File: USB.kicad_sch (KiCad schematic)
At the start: 8 parts

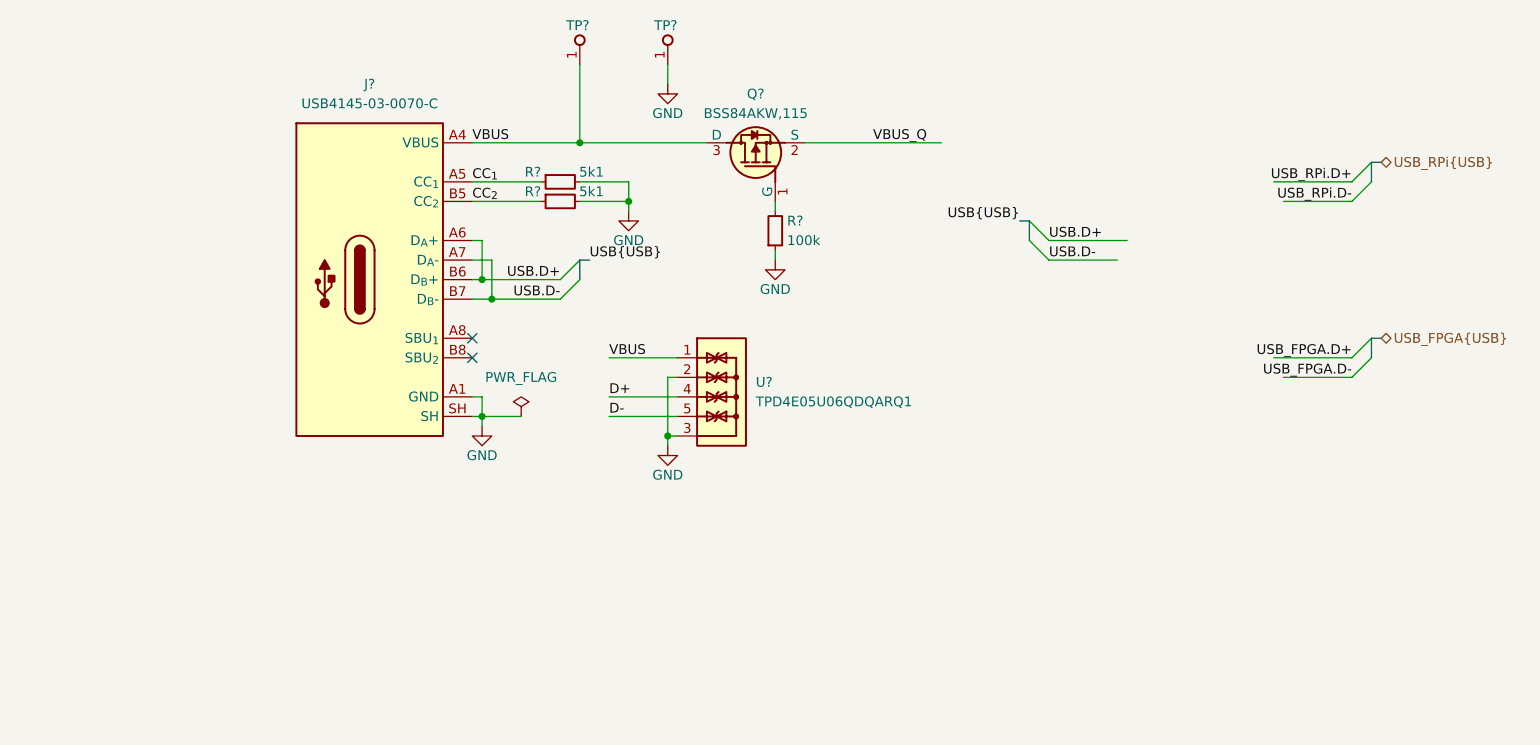
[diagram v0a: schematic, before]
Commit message: [#72133] Add USB mux
Signed-off-by: Dawid Lentka <dlentka@antmicro.com>
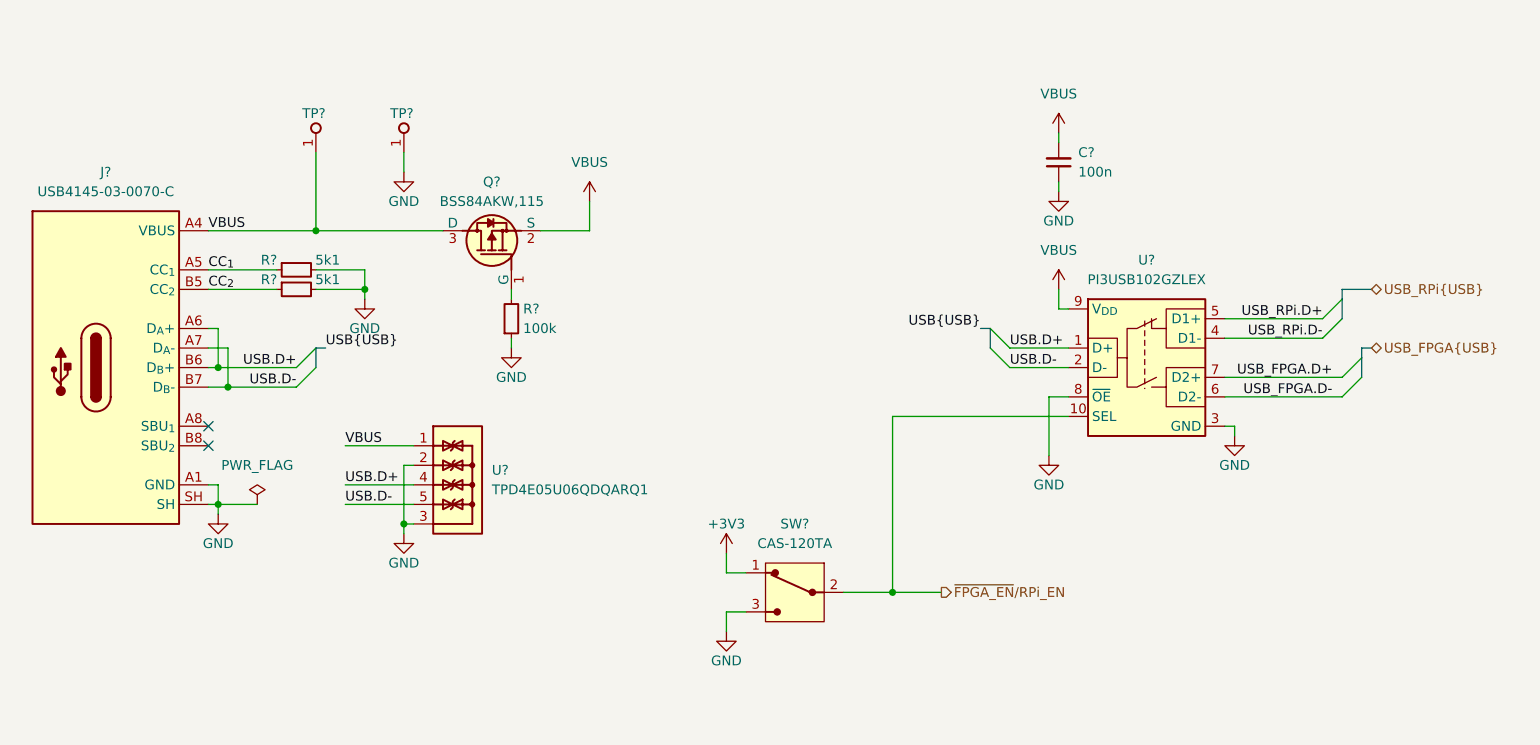
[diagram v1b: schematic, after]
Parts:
- added C?: C_100n_0402, antmicro-footprints:C_0402_1005Metric, symbol antmicroCapacitors0402:C_100n_0402
- added SW?: CAS-120TA, antmicro-footprints:Switch_Slide_CAS-120TA, symbol antmicroSlideSwitches:CAS-120TA
- added U?: PI3USB102GZLEX, antmicro-footprints:UQFN-10_1.4x1.8x0.5mm_P0.4mm, symbol antmicroInterfaceAnalogSwitchesSpecialPurpose:PI3USB102GZLEX
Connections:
- net D+ is gone; now on net USB.D+: U?.4, U?.7
- net D- is gone; now on net USB.D-: U?.5, U?.6
- net VBUS_Q is gone; now on net VBUS: Q?.2 (S)
- net GND: now also C?.1, SW?.3, U?.3 (GND), U?.8 (~{OE})
- net USB.D+: now also U?.1 (D+)
- net USB.D-: now also U?.2 (D-)
- net USB_FPGA.D+: now also U?.7 (D2+)
- net USB_FPGA.D-: now also U?.6 (D2-)
- net USB_RPi.D+: now also U?.5 (D1+)
- net USB_RPi.D-: now also U?.4 (D1-)
- net VBUS: now also C?.2, U?.9 (V_{DD})
- new net +3V3: SW?.1
- new net ~{FPGA_EN}/RPi_EN: SW?.2, U?.10 (SEL)
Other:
- moved on the sheet: J?, Q?, R?, TP?, U?

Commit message: [#72133] Move executor switching to new scheet; Add FPGA flash programmer
Signed-off-by: Dawid Lentka <dlentka@antmicro.com>
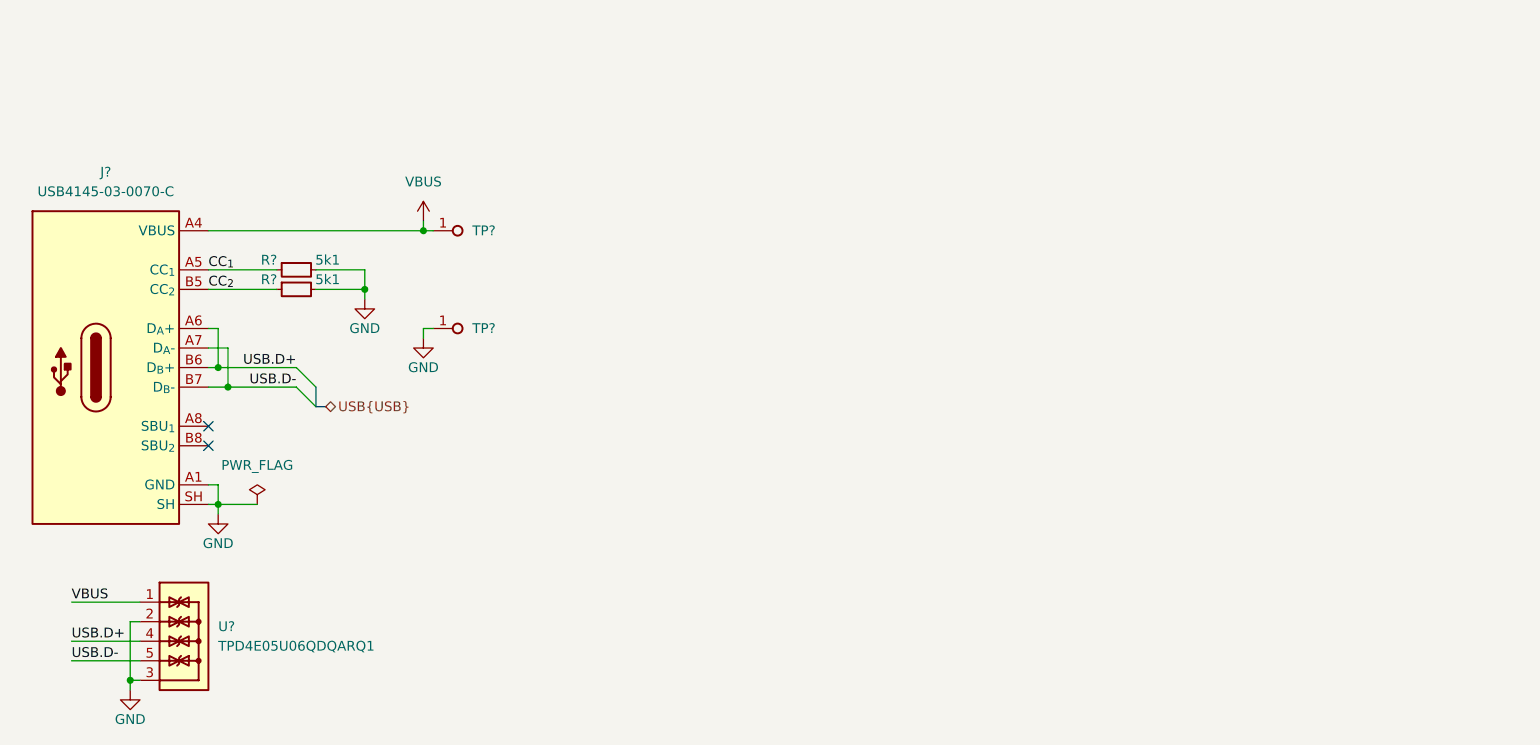
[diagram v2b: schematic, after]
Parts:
- removed C?: C_100n_0402, antmicro-footprints:C_0402_1005Metric, symbol antmicroCapacitors0402:C_100n_0402
- removed Q?: BSS84AKW, antmicro-footprints:SOT-323, symbol antmicroTransistorsFETsMOSFETsSingle:BSS84AKW
- removed R?: R_100k_0402, antmicro-footprints:R_0402_1005Metric, symbol antmicroResistors0402:R_100k_0402
- removed SW?: CAS-120TA, antmicro-footprints:Switch_Slide_CAS-120TA, symbol antmicroSlideSwitches:CAS-120TA
- removed U?: PI3USB102GZLEX, antmicro-footprints:UQFN-10_1.4x1.8x0.5mm_P0.4mm, symbol antmicroInterfaceAnalogSwitchesSpecialPurpose:PI3USB102GZLEX
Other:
- moved on the sheet: TP?, U?

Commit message: [#72133] Unify sheet size
Signed-off-by: Dawid Lentka <dlentka@antmicro.com>
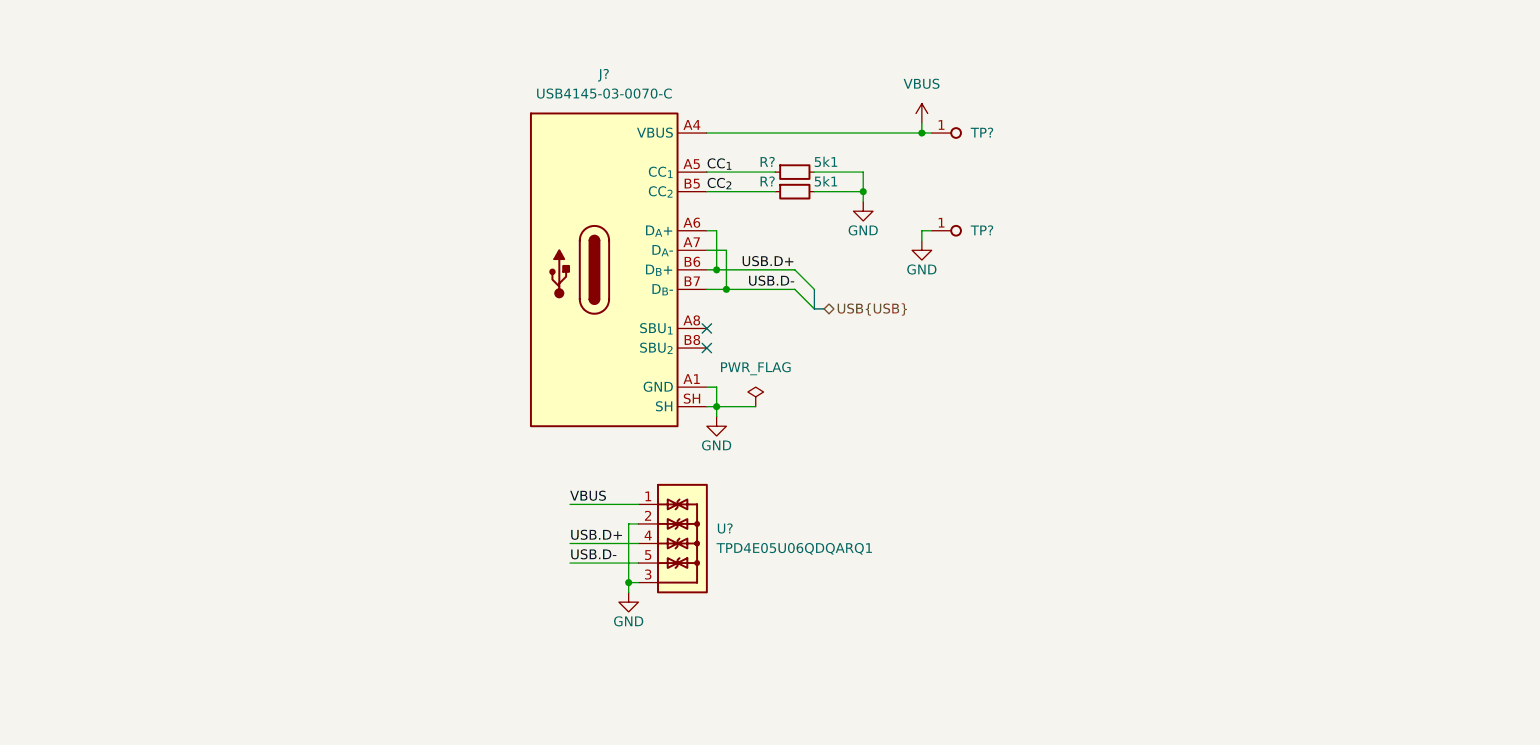
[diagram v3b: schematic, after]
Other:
- title: (none) -> LED Panel Board
- moved on the sheet: J?, R?, TP?, U?

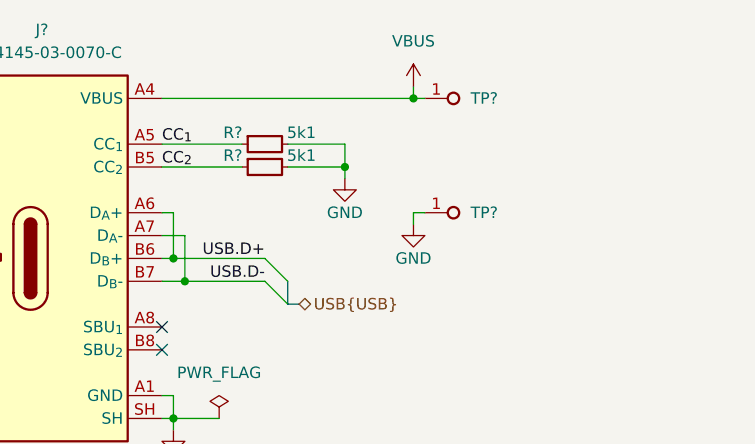
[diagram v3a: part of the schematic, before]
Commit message: [#72133] Add indicator LEDs & testpoints
Signed-off-by: Dawid Lentka <dlentka@antmicro.com>
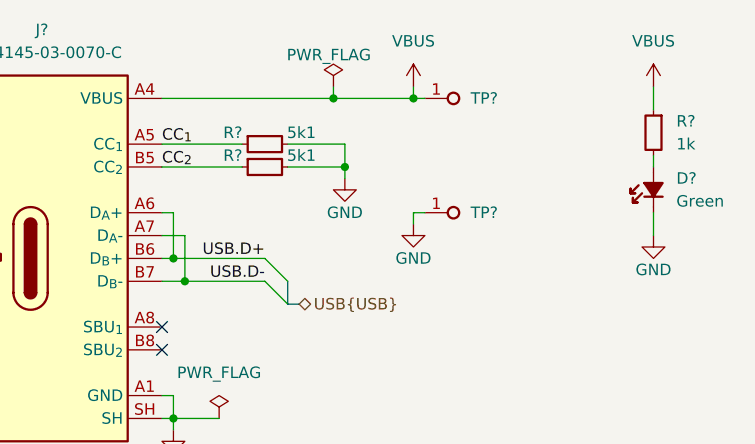
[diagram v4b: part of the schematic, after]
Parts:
- added D?: LED_G_0603_KP-1608CGCK, antmicro-footprints:LED_0603_1608Metric_G, symbol antmicroLEDIndicationDiscrete:LED_G_0603_KP-1608CGCK
- added R?: R_1k_0402, antmicro-footprints:R_0402_1005Metric, symbol antmicroResistors0402:R_1k_0402
- TP? (x2): value TP_1mm_SMD -> TP_0.75mm_SMD; footprint antmicro-footprints:TP_SMD_1mm -> antmicro-footprints:TP_SMD_0.75mm; symbol antmicroTestPoints:TP_1mm_SMD -> antmicroTestPoints:TP_0.75mm_SMD
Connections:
- net GND: now also D?.1 (C)
- net VBUS: now also R?.1
- new net: D?.2 (A), R?.2

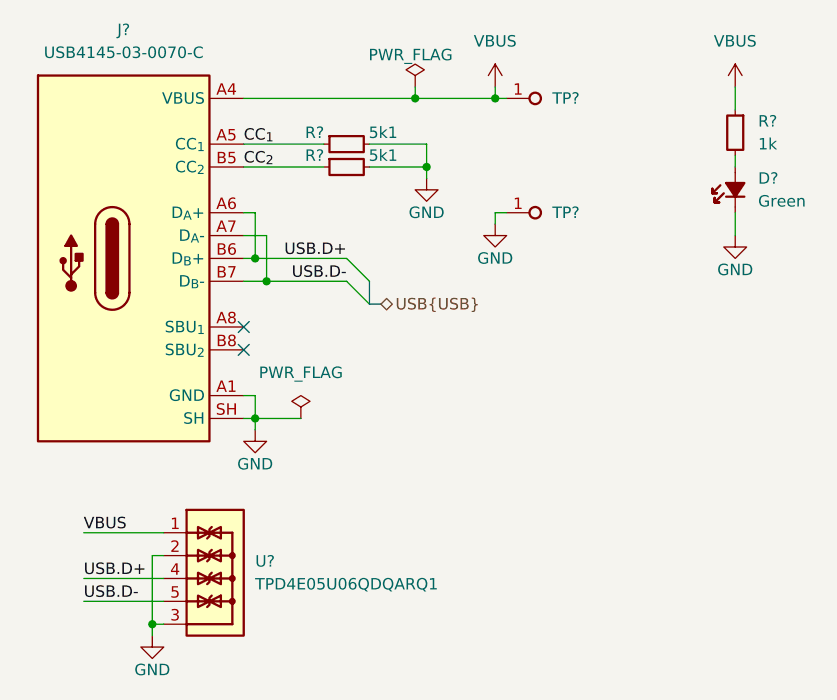
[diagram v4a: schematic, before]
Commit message: [#72133] Annotate schematics
Signed-off-by: Dawid Lentka <dlentka@antmicro.com>
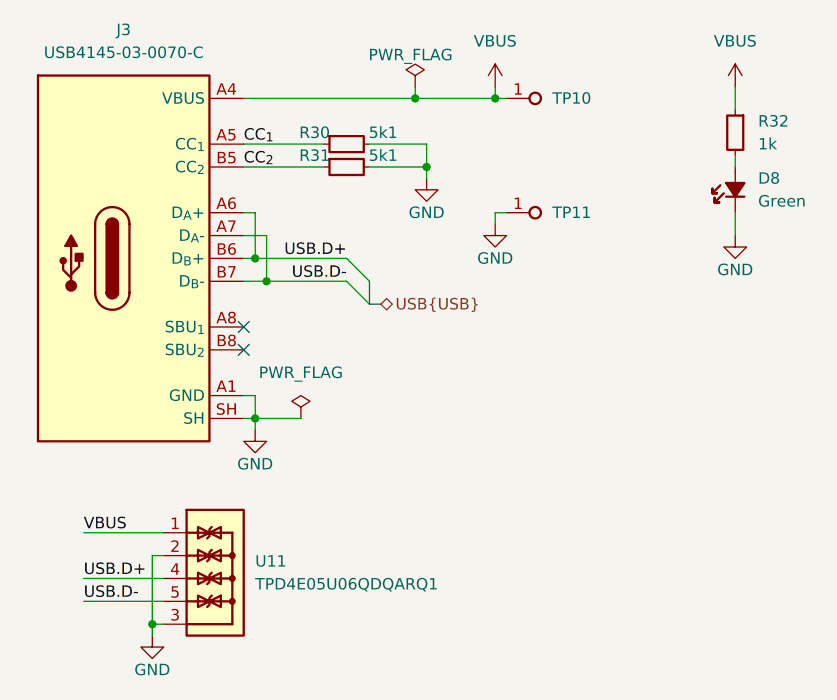
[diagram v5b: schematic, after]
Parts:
- gave numbers to parts that had none: 8
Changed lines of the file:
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@@
 		(dnp no)
 		(fields_autoplaced yes)
-		(property "Reference" "TP?"
+		(property "Reference" "TP10"
 			(at 184.15 74.93 0)
 			(effects
@@
 			(project "led-panel"
 				(path "/a86e1cab-ea0a-45e6-9194-d44b0d5c9450/4155e8b1-3e20-438f-8975-680719ad641f"
-					(reference "TP?")
+					(reference "TP10")
 					(unit 1)
 				)
@@
 		(on_board yes)
 		(dnp no)
-		(property "Reference" "#FLG01"
+		(property "Reference" "#FLG02"
 			(at 168.91 71.755 0)
 			(effects
@@
 			(project ""
 				(path "/a86e1cab-ea0a-45e6-9194-d44b0d5c9450/4155e8b1-3e20-438f-8975-680719ad641f"
-					(reference "#FLG01")
+					(reference "#FLG02")
 					(unit 1)
 				)
@@
 		(dnp no)
 		(fields_autoplaced yes)
-		(property "Reference" "R?"
+		(property "Reference" "R32"
 			(at 207.01 77.47 90)
 			(effects
@@
 			(project "led-panel"
 				(path "/a86e1cab-ea0a-45e6-9194-d44b0d5c9450/4155e8b1-3e20-438f-8975-680719ad641f"
-					(reference "R?")
+					(reference "R32")
 					(unit 1)
 				)
@@
 		(on_board yes)
 		(dnp no)
-		(property "Reference" "#PWR084"
+		(property "Reference" "#PWR0108"
 			(at 160.02 114.3 0)
 			(effects
@@
 			(project "led-panel"
 				(path "/a86e1cab-ea0a-45e6-9194-d44b0d5c9450/4155e8b1-3e20-438f-8975-680719ad641f"
-					(reference "#PWR084")
+					(reference "#PWR0108")
 					(unit 1)
 				)
@@
 		(on_board yes)
 		(dnp no)
-		(property "Reference" "#PWR0200"
+		(property "Reference" "#PWR0113"
 			(at 213.36 92.71 0)
 			(effects
@@
 			(project "led-panel"
 				(path "/a86e1cab-ea0a-45e6-9194-d44b0d5c9450/4155e8b1-3e20-438f-8975-680719ad641f"
-					(reference "#PWR0200")
+					(reference "#PWR0113")
 					(unit 1)
 				)
@@
 		(on_board yes)
 		(dnp no)
-		(property "Reference" "#PWR087"
+		(property "Reference" "#PWR0107"
 			(at 148.59 137.16 0)
 			(effects
@@
 			(project "led-panel"
 				(path "/a86e1cab-ea0a-45e6-9194-d44b0d5c9450/4155e8b1-3e20-438f-8975-680719ad641f"
-					(reference "#PWR087")
+					(reference "#PWR0107")
 					(unit 1)
 				)
@@
 		(on_board yes)
 		(dnp no)
-		(property "Reference" "#PWR085"
+		(property "Reference" "#PWR0109"
 			(at 179.07 86.36 0)
 			(effects
@@
 			(project "led-panel"
 				(path "/a86e1cab-ea0a-45e6-9194-d44b0d5c9450/4155e8b1-3e20-438f-8975-680719ad641f"
-					(reference "#PWR085")
+					(reference "#PWR0109")
 					(unit 1)
 				)
@@
 		(on_board yes)
 		(dnp no)
-		(property "Reference" "R?"
+		(property "Reference" "R30"
 			(at 157.734 78.74 0)
 			(effects
@@
 			(project "led-panel"
 				(path "/a86e1cab-ea0a-45e6-9194-d44b0d5c9450/4155e8b1-3e20-438f-8975-680719ad641f"
-					(reference "R?")
+					(reference "R30")
 					(unit 1)
 				)
@@
 		(dnp no)
 		(fields_autoplaced yes)
-		(property "Reference" "#PWR090"
+		(property "Reference" "#PWR0110"
 			(at 177.8 77.47 0)
 			(effects
@@
 			(project ""
 				(path "/a86e1cab-ea0a-45e6-9194-d44b0d5c9450/4155e8b1-3e20-438f-8975-680719ad641f"
-					(reference "#PWR090")
+					(reference "#PWR0110")
 					(unit 1)
 				)
@@
 		(on_board yes)
 		(dnp no)
-		(property "Reference" "R?"
+		(property "Reference" "R31"
 			(at 157.734 81.28 0)
 			(effects
@@
 			(project "led-panel"
 				(path "/a86e1cab-ea0a-45e6-9194-d44b0d5c9450/4155e8b1-3e20-438f-8975-680719ad641f"
-					(reference "R?")
+					(reference "R31")
 					(unit 1)
 				)
@@
 		(dnp no)
 		(fields_autoplaced yes)
-		(property "Reference" "D?"
+		(property "Reference" "D8"
 			(at 207.01 83.82 90)
 			(effects
@@
 			(project "led-panel"
 				(path "/a86e1cab-ea0a-45e6-9194-d44b0d5c9450/4155e8b1-3e20-438f-8975-680719ad641f"
-					(reference "D?")
+					(reference "D8")
 					(unit 1)
 				)
@@
 		(dnp no)
 		(fields_autoplaced yes)
-		(property "Reference" "J?"
+		(property "Reference" "J3"
 			(at 136.525 67.31 0)
 			(effects
@@
 			(project "led-panel"
 				(path "/a86e1cab-ea0a-45e6-9194-d44b0d5c9450/4155e8b1-3e20-438f-8975-680719ad641f"
-					(reference "J?")
+					(reference "J3")
 					(unit 1)
 				)
@@
 		(dnp no)
 		(fields_autoplaced yes)
-		(property "Reference" "#PWR0199"
+		(property "Reference" "#PWR0112"
 			(at 204.47 77.47 0)
 			(effects
@@
 			(project "led-panel"
 				(path "/a86e1cab-ea0a-45e6-9194-d44b0d5c9450/4155e8b1-3e20-438f-8975-680719ad641f"
-					(reference "#PWR0199")
+					(reference "#PWR0112")
 					(unit 1)
 				)
@@
 		(dnp no)
 		(fields_autoplaced yes)
-		(property "Reference" "#FLG02"
+		(property "Reference" "#FLG01"
 			(at 156.21 108.585 0)
 			(effects
@@
 			(project "led-panel"
 				(path "/a86e1cab-ea0a-45e6-9194-d44b0d5c9450/4155e8b1-3e20-438f-8975-680719ad641f"
-					(reference "#FLG02")
+					(reference "#FLG01")
 					(unit 1)
 				)
@@
 		(on_board yes)
 		(dnp no)
-		(property "Reference" "#PWR086"
+		(property "Reference" "#PWR0111"
 			(at 186.69 91.44 0)
 			(effects
@@
 			(project "led-panel"
 				(path "/a86e1cab-ea0a-45e6-9194-d44b0d5c9450/4155e8b1-3e20-438f-8975-680719ad641f"
-					(reference "#PWR086")
+					(reference "#PWR0111")
 					(unit 1)
 				)
@@
 		(dnp no)
 		(fields_autoplaced yes)
-		(property "Reference" "TP?"
+		(property "Reference" "TP11"
 			(at 184.15 87.63 0)
 			(effects
@@
 			(project "led-panel"
 				(path "/a86e1cab-ea0a-45e6-9194-d44b0d5c9450/4155e8b1-3e20-438f-8975-680719ad641f"
-					(reference "TP?")
+					(reference "TP11")
 					(unit 1)
 				)
@@
 		(dnp no)
 		(fields_autoplaced yes)
-		(property "Reference" "U?"
+		(property "Reference" "U11"
 			(at 151.13 126.365 0)
 			(effects
@@
 			(project "led-panel"
 				(path "/a86e1cab-ea0a-45e6-9194-d44b0d5c9450/4155e8b1-3e20-438f-8975-680719ad641f"
-					(reference "U?")
+					(reference "U11")
 					(unit 1)
 				)
